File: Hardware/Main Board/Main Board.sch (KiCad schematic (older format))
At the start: 54 parts, among them Q1 MMBT3904-TP, Q2 MMBT3904-TP, Q3 AO4484, SW1 Momentary, U1 MT3608, U2 NCP718A, U3 ATtiny1614, U4 TP4056

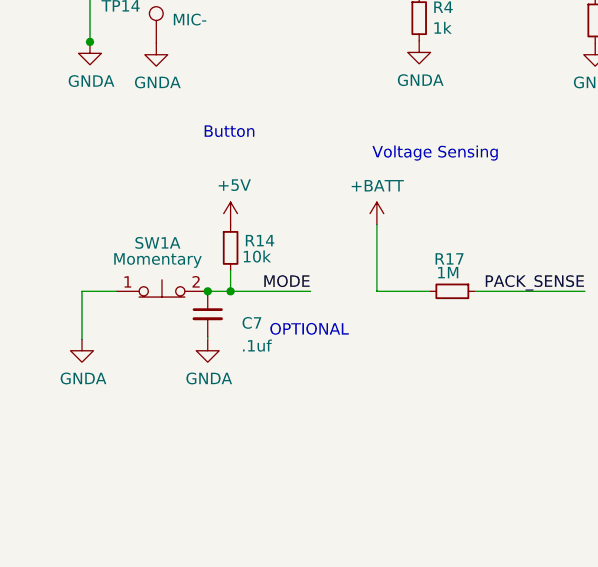
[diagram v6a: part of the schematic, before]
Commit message: board review done, almost done BOM and component map.
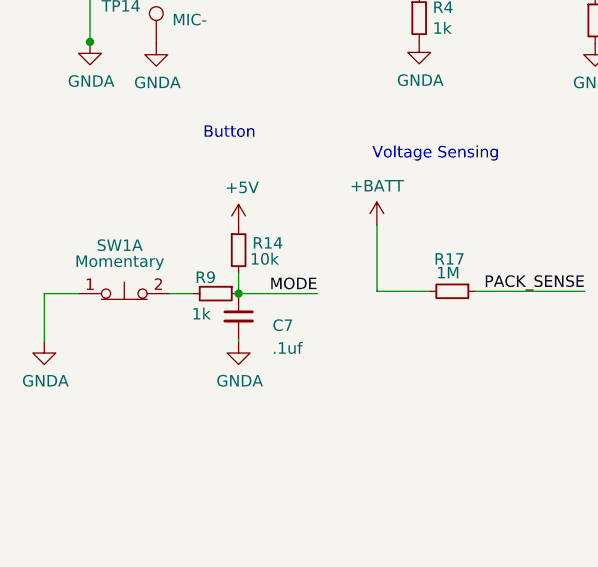
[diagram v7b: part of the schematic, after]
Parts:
- added R9: 1k, Resistor_SMD:R_0603_1608Metric, symbol Device:R_Small
- C1, C2, C3: footprint Main Board:CP_Elec_4x3 -> Capacitor_SMD:CP_Elec_4x5.3
- C5, C6: footprint Main Board:100 -> Capacitor_SMD:CP_Elec_6.3x7.7
- FB1: footprint Resistor_SMD:R_0805_2012Metric -> Resistor_SMD:R_0603_1608Metric
- L1: footprint Main Board:BW10uHInductor -> Inductor_SMD:L_Sunlord_MWSA0518_5.4x5.2mm
- SW1: footprint Button_Switch_SMD:SW_SPST_PTS645 -> Main Board1:tactile
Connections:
- wire segments 134 -> 135
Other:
- note removed: "OPTIONAL\n"
- moved on the sheet: C7, R14, SW1A
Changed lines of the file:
@@
 EESchema Schematic File Version 4
-LIBS:Main Board-cache
 EELAYER 30 0
 EELAYER END
@@
 F 0 "C3" V 3608 4460 50  0000 C CNN
 F 1 "10uf" V 3517 4460 50  0000 C CNN
-F 2 "Main Board:CP_Elec_4x3" H 3380 4460 50  0001 C CNN
+F 2 "Capacitor_SMD:CP_Elec_4x5.3" H 3380 4460 50  0001 C CNN
 F 3 "~" H 3380 4460 50  0001 C CNN
 	1    3380 4460
@@
 F 0 "C2" V 2738 4660 50  0000 C CNN
 F 1 "10uf" V 2647 4660 50  0000 C CNN
-F 2 "Main Board:CP_Elec_4x3" H 2510 4660 50  0001 C CNN
+F 2 "Capacitor_SMD:CP_Elec_4x5.3" H 2510 4660 50  0001 C CNN
 F 3 "~" H 2510 4660 50  0001 C CNN
 	1    2510 4660
@@
 Button\n
 $Comp
-L Device:R_Small R14
-U 1 1 5ECB70F4
-P 1385 6165
-F 0 "R14" H 1445 6195 50  0000 L CNN
-F 1 "10k" H 1435 6125 50  0000 L CNN
-F 2 "Resistor_SMD:R_0603_1608Metric" H 1385 6165 50  0001 C CNN
-F 3 "~" H 1385 6165 50  0001 C CNN
-	1    1385 6165
-	1    0    0    -1
-$EndComp
-$Comp
-L power:+5V #PWR019
-U 1 1 5ECB83BC
-P 1385 6065
-F 0 "#PWR019" H 1385 5915 50  0001 C CNN
-F 1 "+5V" H 1400 6238 50  0000 C CNN
-F 2 "" H 1385 6065 50  0001 C CNN
-F 3 "" H 1385 6065 50  0001 C CNN
-	1    1385 6065
-	1    0    0    -1
-$EndComp
-$Comp
 L Switch:SW_Push_Open_Dual_x2 SW1
 U 1 1 5ECC37E1
-P 1085 6355
-F 0 "SW1" H 1065 6565 50  0000 C CNN
-F 1 "Momentary" H 1065 6495 50  0000 C CNN
-F 2 "Button_Switch_SMD:SW_SPST_PTS645" H 1085 6555 50  0001 C CNN
-F 3 "~" H 1085 6555 50  0001 C CNN
-	1    1085 6355
-	1    0    0    -1
-$EndComp
-Wire Wire Line
-	735  6355 885  6355
-Text Label 1735 6355 2    50   ~ 0
+P 920 6365
+F 0 "SW1" H 900 6575 50  0000 C CNN
+F 1 "Momentary" H 900 6505 50  0000 C CNN
+F 2 "Main Board1:tactile" H 920 6565 50  0001 C CNN
+F 3 "~" H 920 6565 50  0001 C CNN
+	1    920  6365
+	1    0    0    -1
+$EndComp
+Text Label 1765 6365 2    50   ~ 0
 MODE
 $Comp
@@
 $EndComp
 Wire Wire Line
-	735  6355 735  6565
-Wire Wire Line
-	1385 6265 1385 6355
-Wire Wire Line
-	1285 6355 1385 6355
-Wire Wire Line
-	1385 6355 1735 6355
-Connection ~ 1385 6355
+	1120 6365 1220 6365
 $Comp
 L Device:D_Zener D3
@@
 F 0 "L1" V 1770 2580 50  0000 C CNN
 F 1 "10uh" V 1679 2580 50  0000 C CNN
-F 2 "Main Board:BW10uHInductor" H 1545 2580 50  0001 C CNN
+F 2 "Inductor_SMD:L_Sunlord_MWSA0518_5.4x5.2mm" H 1545 2580 50  0001 C CNN
 F 3 "~" H 1545 2580 50  0001 C CNN
 	1    1545 2580
@@
 F 0 "C5" H 3295 2670 50  0000 L CNN
 F 1 "100uf" H 3265 2590 50  0000 L CNN
-F 2 "Main Board:100" H 3515 2680 50  0001 C CNN
+F 2 "Capacitor_SMD:CP_Elec_6.3x7.7" H 3515 2680 50  0001 C CNN
 F 3 "~" H 3515 2680 50  0001 C CNN
 	1    3515 2680
@@
 	4295 6525 4295 6555
 $Comp
-L power:GNDA #PWR04
-U 1 1 5F234ADB
-P 735 6565
-F 0 "#PWR04" H 735 6315 50  0001 C CNN
-F 1 "GNDA" H 740 6392 50  0000 C CNN
-F 2 "" H 735 6565 50  0001 C CNN
-F 3 "" H 735 6565 50  0001 C CNN
-	1    735  6565
-	1    0    0    -1
-$EndComp
-$Comp
 L power:GNDA #PWR014
 U 1 1 5F238051
@@
 F 0 "FB1" V 2898 3205 50  0000 C CNN
 F 1 "ACML-0805-190-T" V 2989 3205 50  0000 C CNN
-F 2 "Resistor_SMD:R_0805_2012Metric" V 3065 3205 50  0001 C CNN
+F 2 "Resistor_SMD:R_0603_1608Metric" V 3065 3205 50  0001 C CNN
 F 3 "~" H 3135 3205 50  0001 C CNN
 	1    3135 3205
@@
 	1    0    0    -1
 $EndComp
-$Comp
-L Device:CP1_Small C6
-U 1 1 5EE78E32
-P 770 4295
-F 0 "C6" H 890 4350 50  0000 C CNN
-F 1 "100uf" H 945 4275 50  0000 C CNN
-F 2 "Main Board:100" H 770 4295 50  0001 C CNN
-F 3 "~" H 770 4295 50  0001 C CNN
-	1    770  4295
-	1    0    0    -1
-$EndComp
 Wire Wire Line
 	1060 4120 1060 4195
@@
 L Device:C_Small C7
 U 1 1 5EF7EC11
-P 1285 6455
-F 0 "C7" H 1045 6415 50  0000 L CNN
-F 1 ".1uf" H 1005 6315 50  0000 L CNN
-F 2 "Capacitor_SMD:C_0603_1608Metric" H 1285 6455 50  0001 C CNN
-F 3 "~" H 1285 6455 50  0001 C CNN
-	1    1285 6455
+P 1420 6465
+F 0 "C7" H 1180 6425 50  0000 L CNN
+F 1 ".1uf" H 1140 6325 50  0000 L CNN
+F 2 "Capacitor_SMD:C_0603_1608Metric" H 1420 6465 50  0001 C CNN
+F 3 "~" H 1420 6465 50  0001 C CNN
+	1    1420 6465
 	-1   0    0    -1
 $EndComp
@@
 L power:GNDA #PWR0101
 U 1 1 5EF7FD8D
-P 1285 6565
-F 0 "#PWR0101" H 1285 6315 50  0001 C CNN
-F 1 "GNDA" H 1290 6392 50  0000 C CNN
-F 2 "" H 1285 6565 50  0001 C CNN
-F 3 "" H 1285 6565 50  0001 C CNN
-	1    1285 6565
-	1    0    0    -1
-$EndComp
-Connection ~ 1285 6355
-Wire Wire Line
-	1285 6555 1285 6565
+P 1420 6575
+F 0 "#PWR0101" H 1420 6325 50  0001 C CNN
+F 1 "GNDA" H 1425 6402 50  0000 C CNN
+F 2 "" H 1420 6575 50  0001 C CNN
+F 3 "" H 1420 6575 50  0001 C CNN
+	1    1420 6575
+	1    0    0    -1
+$EndComp
+Wire Wire Line
+	1420 6565 1420 6575
 $Comp
 L Device:C_Small C12
@@
 Wire Wire Line
 	4045 4460 4360 4460
-Text Notes 1555 6560 0    50   ~ 0
-OPTIONAL\n
 Wire Wire Line
 	4362 2980 4362 3292
@@
 Wire Wire Line
 	890  2780 890  3295
-$Comp
-L Device:CP1_Small C1
-U 1 1 5EB25AD7
-P 1490 4860
-F 0 "C1" V 1718 4860 50  0000 C CNN
-F 1 "10uf" V 1627 4860 50  0000 C CNN
-F 2 "Main Board:CP_Elec_4x3" H 1490 4860 50  0001 C CNN
-F 3 "~" H 1490 4860 50  0001 C CNN
-	1    1490 4860
-	0    -1   -1   0
-$EndComp
-Wire Wire Line
-	1060 4860 1390 4860
-Wire Wire Line
-	1390 4860 1392 4860
-Connection ~ 1390 4860
 Wire Wire Line
 	1060 4720 1060 4858
@@
 NoConn ~ 8010 4200
 NoConn ~ 8010 4400
+$Comp
+L Device:R_Small R9
+U 1 1 5F24F16D
+P 1320 6365
+F 0 "R9" V 1250 6275 50  0000 L CNN
+F 1 "1k" V 1410 6260 50  0000 L CNN
+F 2 "Resistor_SMD:R_0603_1608Metric" H 1320 6365 50  0001 C CNN
+F 3 "~" H 1320 6365 50  0001 C CNN
+	1    1320 6365
+	0    1    1    0
+$EndComp
+$Comp
+L power:GNDA #PWR04
+U 1 1 5F234ADB
+P 570 6575
+F 0 "#PWR04" H 570 6325 50  0001 C CNN
+F 1 "GNDA" H 575 6402 50  0000 C CNN
+F 2 "" H 570 6575 50  0001 C CNN
+F 3 "" H 570 6575 50  0001 C CNN
+	1    570  6575
+	1    0    0    -1
+$EndComp
+Wire Wire Line
+	570  6365 570  6575
+Wire Wire Line
+	570  6365 720  6365
+Wire Wire Line
+	1415 6365 1420 6365
+Wire Wire Line
+	1420 6275 1420 6365
+$Comp
+L power:+5V #PWR019
+U 1 1 5ECB83BC
+P 1420 6075
+F 0 "#PWR019" H 1420 5925 50  0001 C CNN
+F 1 "+5V" H 1435 6248 50  0000 C CNN
+F 2 "" H 1420 6075 50  0001 C CNN
+F 3 "" H 1420 6075 50  0001 C CNN
+	1    1420 6075
+	1    0    0    -1
+$EndComp
+$Comp
+L Device:R_Small R14
+U 1 1 5ECB70F4
+P 1420 6175
+F 0 "R14" H 1480 6205 50  0000 L CNN
+F 1 "10k" H 1470 6135 50  0000 L CNN
+F 2 "Resistor_SMD:R_0603_1608Metric" H 1420 6175 50  0001 C CNN
+F 3 "~" H 1420 6175 50  0001 C CNN
+	1    1420 6175
+	1    0    0    -1
+$EndComp
+Connection ~ 1420 6365
+Wire Wire Line
+	1420 6365 1765 6365
+$Comp
+L Device:CP1_Small C6
+U 1 1 5EE78E32
+P 770 4295
+F 0 "C6" H 890 4350 50  0000 C CNN
+F 1 "100uf" H 945 4275 50  0000 C CNN
+F 2 "Capacitor_SMD:CP_Elec_6.3x7.7" H 770 4295 50  0001 C CNN
+F 3 "~" H 770 4295 50  0001 C CNN
+	1    770  4295
+	1    0    0    -1
+$EndComp
+Connection ~ 1390 4860
+Wire Wire Line
+	1390 4860 1392 4860
+Wire Wire Line
+	1060 4860 1390 4860
+$Comp
+L Device:CP1_Small C1
+U 1 1 5EB25AD7
+P 1490 4860
+F 0 "C1" V 1718 4860 50  0000 C CNN
+F 1 "10uf" V 1627 4860 50  0000 C CNN
+F 2 "Capacitor_SMD:CP_Elec_4x5.3" H 1490 4860 50  0001 C CNN
+F 3 "~" H 1490 4860 50  0001 C CNN
+	1    1490 4860
+	0    -1   -1   0
+$EndComp
 $EndSCHEMATC

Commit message: board sent for production
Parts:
- C12, C4: footprint Capacitor_SMD:C_0603_1608Metric -> Capacitor_SMD:C_0805_2012Metric
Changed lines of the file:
@@
 F 0 "C4" H 2595 2580 50  0000 L CNN
 F 1 "22uf" H 2525 2495 50  0000 L CNN
-F 2 "Capacitor_SMD:C_0603_1608Metric" H 2765 2680 50  0001 C CNN
+F 2 "Capacitor_SMD:C_0805_2012Metric" H 2765 2680 50  0001 C CNN
 F 3 "~" H 2765 2680 50  0001 C CNN
 	1    2765 2680
@@
 F 0 "C12" H 1020 2740 50  0000 L CNN
 F 1 "22uf" H 985 2665 50  0000 L CNN
-F 2 "Capacitor_SMD:C_0603_1608Metric" H 890 2680 50  0001 C CNN
+F 2 "Capacitor_SMD:C_0805_2012Metric" H 890 2680 50  0001 C CNN
 F 3 "~" H 890 2680 50  0001 C CNN
 	1    890  2680
